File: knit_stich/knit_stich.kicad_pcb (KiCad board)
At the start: 4 copper layers, 89.5 x 65.2 mm, 0 parts

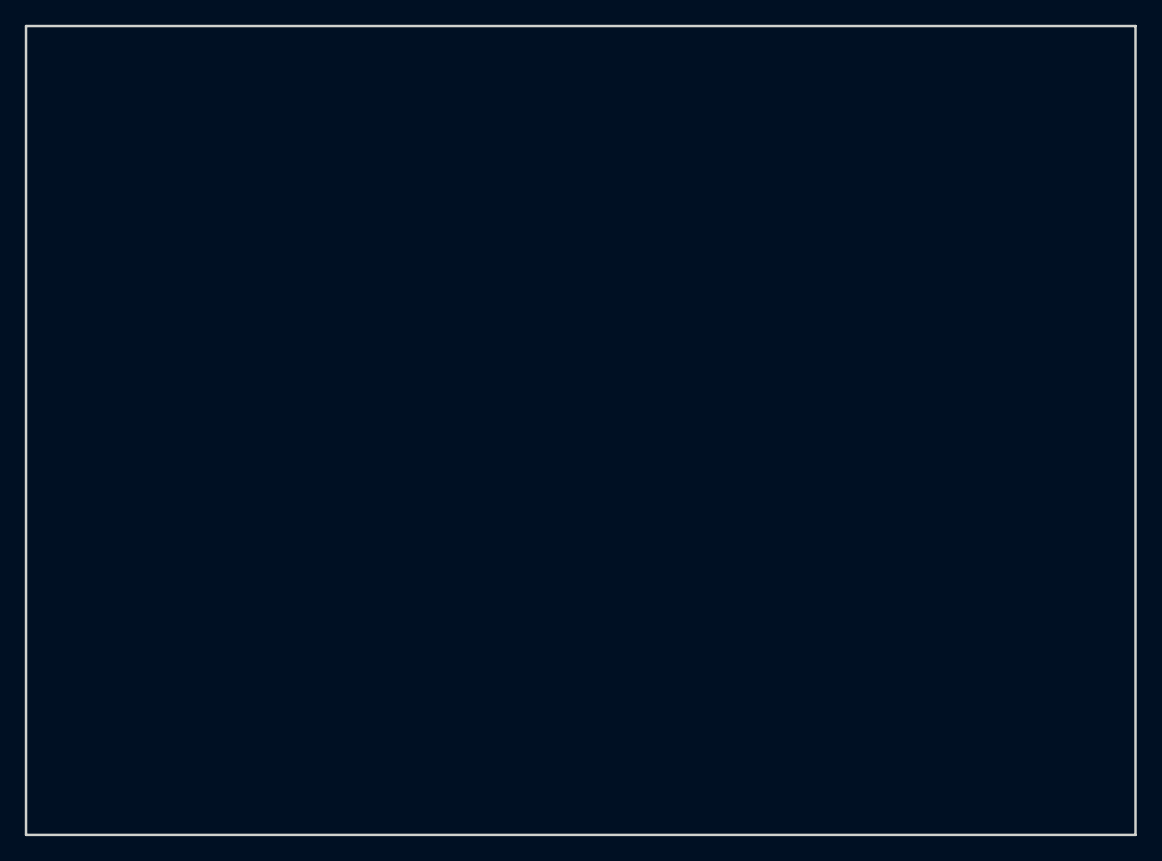
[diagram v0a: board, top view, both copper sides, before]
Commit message: added 2x3 connector
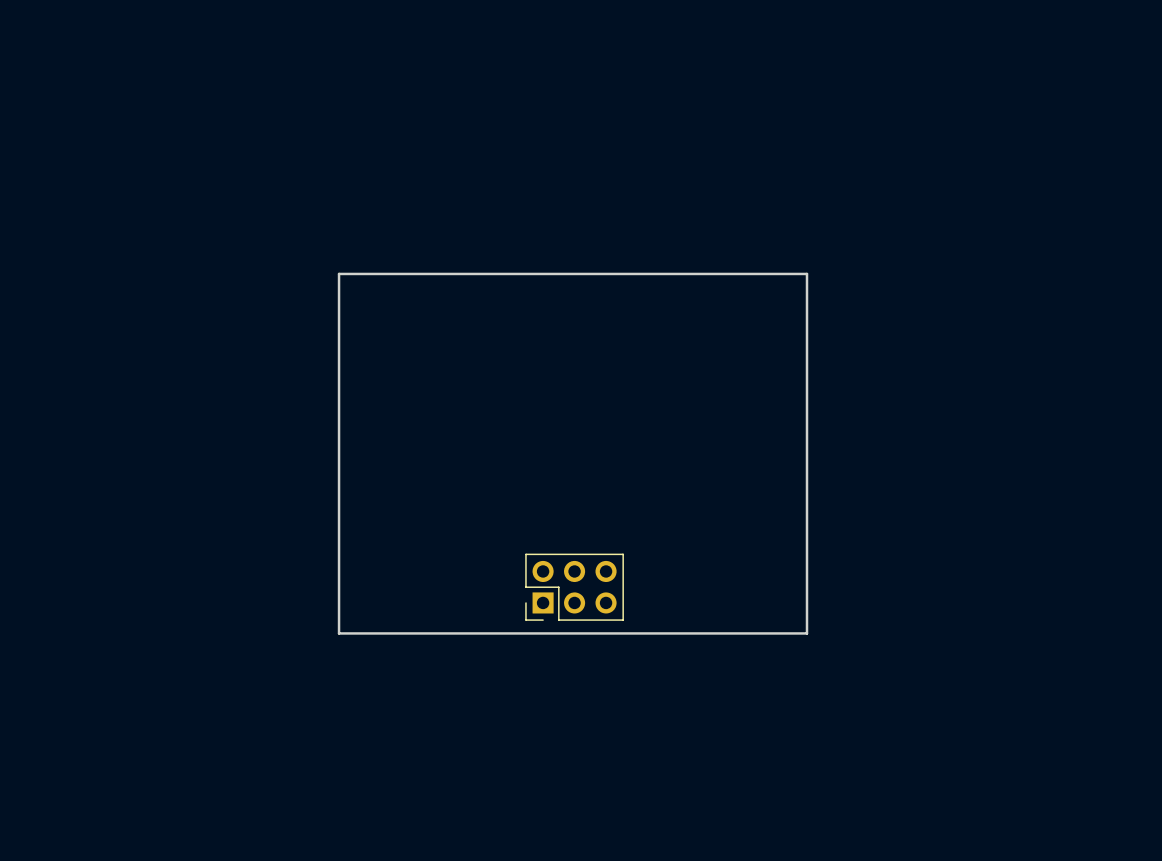
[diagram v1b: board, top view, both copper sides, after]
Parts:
- added J1: Conn_02x03_Counter_Clockwise, Connector_PinHeader_2.54mm:PinHeader_2x03_P2.54mm_Vertical, F.Cu at (158.2, 105.8)
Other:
- board size 89.5 x 65.2 mm -> 37.8 x 29 mm

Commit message: add gitignore
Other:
- board size 37.8 x 29 mm -> 37.2 x 28.2 mm
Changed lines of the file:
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@@
 		(layer "In2.Cu")
 	)
-	(gr_rect
-		(start 141.75 79.25)
-		(end 179.5 108.25)
+	(gr_poly
+		(pts
+			(xy 172.679214 79.411041) (xy 172.875432 79.414604) (xy 173.071511 79.422028) (xy 173.267372 79.434237)
+			(xy 173.462933 79.452156) (xy 173.658117 79.476708) (xy 173.897271 79.513147) (xy 174.133793 79.562787)
+			(xy 174.367398 79.62527) (xy 174.597799 79.700233) (xy 174.824712 79.787317) (xy 175.047851 79.886162)
+			(xy 175.26693 79.996407) (xy 175.481665 80.117691) (xy 175.691769 80.249654) (xy 175.896958 80.391936)
+			(xy 176.291446 80.706013) (xy 176.662846 81.057038) (xy 177.008873 81.442129) (xy 177.327244 81.858401)
+			(xy 177.615676 82.302971) (xy 177.871885 82.772955) (xy 178.093586 83.26547) (xy 178.278498 83.777631)
+			(xy 178.424335 84.306555) (xy 178.528814 84.849359) (xy 178.56483 85.125065) (xy 178.589651 85.403159)
+			(xy 178.613704 88.496238) (xy 178.619149 91.589729) (xy 178.616918 97.776849) (xy 178.60883 98.288336)
+			(xy 178.610099 98.800184) (xy 178.6221 99.824176) (xy 178.62353 100.335926) (xy 178.615711 100.847252)
+			(xy 178.593993 101.357955) (xy 178.553724 101.867841) (xy 178.521001 102.148441) (xy 178.476622 102.425766)
+			(xy 178.420916 102.699481) (xy 178.354209 102.969252) (xy 178.276828 103.234744) (xy 178.189101 103.495622)
+			(xy 178.091355 103.751553) (xy 177.983917 104.0022) (xy 177.867115 104.247229) (xy 177.741275 104.486307)
+			(xy 177.606726 104.719097) (xy 177.463793 104.945266) (xy 177.312806 105.164479) (xy 177.154089 105.3764)
+			(xy 176.987972 105.580697) (xy 176.814781 105.777032) (xy 176.634843 105.965073) (xy 176.448486 106.144485)
+			(xy 176.256036 106.314932) (xy 176.057822 106.47608) (xy 175.85417 106.627595) (xy 175.645408 106.769142)
+			(xy 175.431862 106.900385) (xy 175.213861 107.020991) (xy 174.99173 107.130625) (xy 174.765799 107.228952)
+			(xy 174.536393 107.315638) (xy 174.30384 107.390347) (xy 174.068467 107.452746) (xy 173.830602 107.502499)
+			(xy 173.590572 107.539272) (xy 173.348703 107.56273) (xy 149.886782 107.582055) (xy 149.452176 107.573133)
+			(xy 149.017336 107.574194) (xy 148.147458 107.587189) (xy 147.712674 107.589587) (xy 147.278161 107.582895)
+			(xy 146.844046 107.562343) (xy 146.627177 107.54538) (xy 146.410456 107.523164) (xy 146.16854 107.491112)
+			(xy 145.929226 107.445427) (xy 145.692807 107.386484) (xy 145.459575 107.314657) (xy 145.229822 107.230323)
+			(xy 145.003841 107.133856) (xy 144.781925 107.025631) (xy 144.564366 106.906024) (xy 144.351456 106.77541)
+			(xy 144.143487 106.634164) (xy 143.743546 106.321276) (xy 143.36688 105.970361) (xy 143.01583 105.584423)
+			(xy 142.692736 105.166461) (xy 142.399936 104.719477) (xy 142.139771 104.246473) (xy 141.91458 103.75045)
+			(xy 141.726703 103.234409) (xy 141.578479 102.701352) (xy 141.472247 102.154281) (xy 141.43561 101.876428)
+			(xy 141.410348 101.596196) (xy 141.386236 98.492292) (xy 141.380784 95.387969) (xy 141.383024 89.179183)
+			(xy 141.391341 88.668768) (xy 141.390029 88.157937) (xy 141.377779 87.135922) (xy 141.376471 86.625182)
+			(xy 141.384794 86.114917) (xy 141.407563 85.60535) (xy 141.449593 85.096702) (xy 141.4835 84.817278)
+			(xy 141.52895 84.541165) (xy 141.58562 84.268691) (xy 141.653185 84.000187) (xy 141.731321 83.735983)
+			(xy 141.819704 83.476408) (xy 141.91801 83.221793) (xy 142.025914 82.972468) (xy 142.143093 82.728762)
+			(xy 142.269222 82.491005) (xy 142.403978 82.259529) (xy 142.547036 82.034661) (xy 142.698073 81.816733)
+			(xy 142.856763 81.606075) (xy 143.022784 81.403016) (xy 143.19581 81.207886) (xy 143.375518 81.021016)
+			(xy 143.561584 80.842735) (xy 143.753683 80.673374) (xy 143.951492 80.513261) (xy 144.154687 80.362728)
+			(xy 144.362942 80.222104) (xy 144.575935 80.091719) (xy 144.793341 79.971903) (xy 145.014836 79.862987)
+			(xy 145.240096 79.765299) (xy 145.468797 79.679171) (xy 145.700614 79.604931) (xy 145.935224 79.542911)
+			(xy 146.172303 79.493439) (xy 146.411526 79.456847) (xy 146.652569 79.433463) (xy 172.090525 79.414254)
+			(xy 172.090513 79.414273) (xy 172.482935 79.410414)
+		)
 		(stroke
-			(width 0.2)
+			(width 0.1)
 			(type solid)
+			(color 255 85 85 1)
 		)
 		(fill no)
@@
 		)
 	)
+	(group ""
+		(members "df4445b0-fc9c-452b-98b0-ab519abb0a29")
+	)
 	(embedded_fonts no)

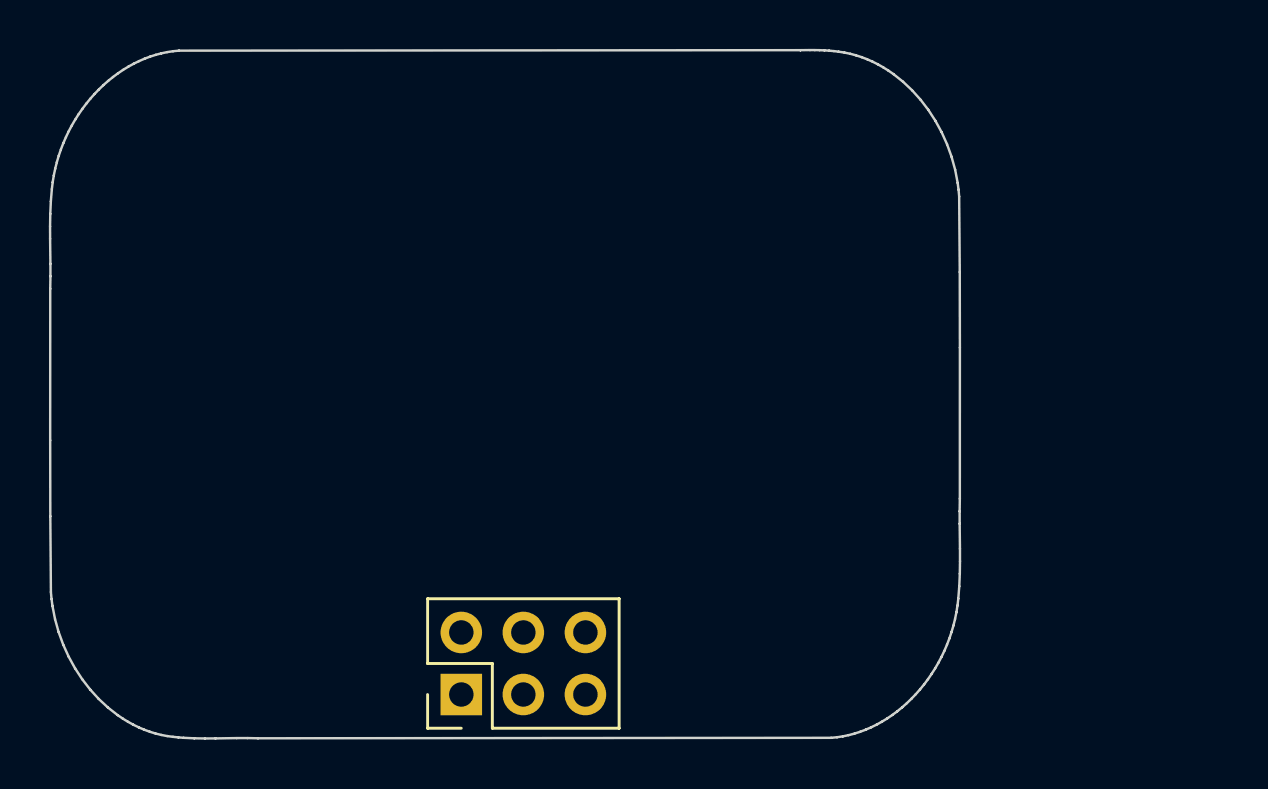
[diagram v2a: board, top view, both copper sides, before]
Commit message: added step for right angle led
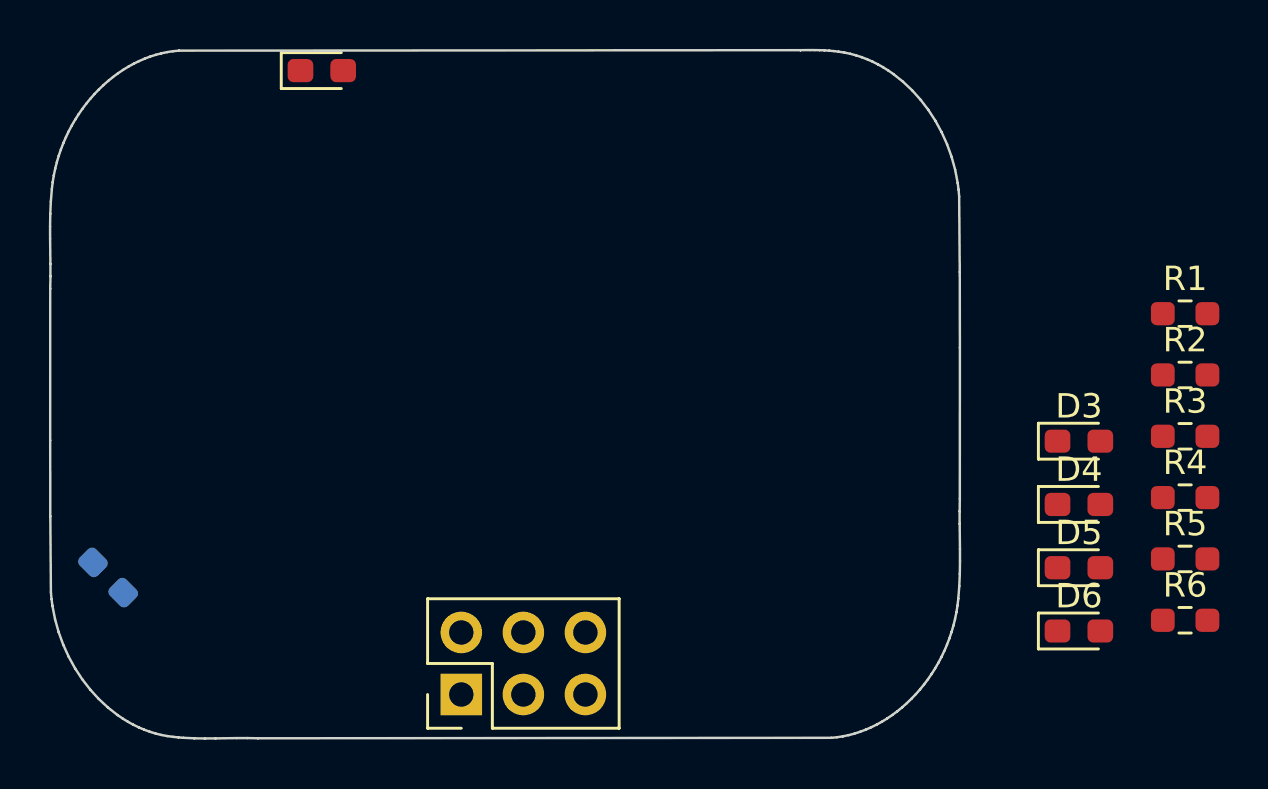
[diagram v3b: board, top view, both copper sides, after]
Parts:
- added D1: LED, LED_SMD:LED_0603_1608Metric_Pad1.05x0.95mm_HandSolder, B.Cu at (143.8, 101.0)
- added D2: LED, LED_SMD:LED_0603_1608Metric_Pad1.05x0.95mm_HandSolder, F.Cu at (152.5, 80.2)
- added D3: LED, LED_SMD:LED_0603_1608Metric_Pad1.05x0.95mm_HandSolder, F.Cu at (183.5, 95.4)
- added D4: LED, LED_SMD:LED_0603_1608Metric_Pad1.05x0.95mm_HandSolder, F.Cu at (183.5, 98.0)
- added D5: LED, LED_SMD:LED_0603_1608Metric_Pad1.05x0.95mm_HandSolder, F.Cu at (183.5, 100.6)
- added D6: LED, LED_SMD:LED_0603_1608Metric_Pad1.05x0.95mm_HandSolder, F.Cu at (183.5, 103.2)
- added R1: R_US, Resistor_SMD:R_0603_1608Metric_Pad0.98x0.95mm_HandSolder, F.Cu at (187.8, 90.2)
- added R2: R_US, Resistor_SMD:R_0603_1608Metric_Pad0.98x0.95mm_HandSolder, F.Cu at (187.8, 92.7)
- added R3: R_US, Resistor_SMD:R_0603_1608Metric_Pad0.98x0.95mm_HandSolder, F.Cu at (187.8, 95.2)
- added R4: R_US, Resistor_SMD:R_0603_1608Metric_Pad0.98x0.95mm_HandSolder, F.Cu at (187.8, 97.7)
- added R5: R_US, Resistor_SMD:R_0603_1608Metric_Pad0.98x0.95mm_HandSolder, F.Cu at (187.8, 100.2)
- added R6: R_US, Resistor_SMD:R_0603_1608Metric_Pad0.98x0.95mm_HandSolder, F.Cu at (187.8, 102.8)
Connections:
- J1 pad 1: unconnected-(J1-Pin_1-Pad1) -> GND
- J1 pad 2: unconnected-(J1-Pin_2-Pad2) -> +3.3V

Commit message: all components in place
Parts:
- D2, D3, D4, D5, D6, R1, R2, R3, R4, R5, R6: moved to B.Cu
- moved R1 45.9 mm to (142.2, 95.2), turned to 90 degrees
- moved R2 40.2 mm to (149.7, 80.0)
- moved R5 38.2 mm to (149.7, 102.2)
- moved D5 29.8 mm to (153.7, 102.2), turned to 180 degrees
- moved R3 23.1 mm to (170.4, 80.0), turned to 180 degrees
- moved D3 23.0 mm to (166.4, 80.0)
- moved R6 17.4 mm to (170.4, 102.2), turned to 180 degrees
- moved D6 17.1 mm to (166.4, 102.2)
- moved R4 10.4 mm to (177.8, 95.2), turned to 90 degrees
- moved D1 9.86 mm to (142.2, 91.2), turned to -90 degrees
- moved D4 8.87 mm to (177.8, 91.2), turned to -90 degrees
- moved D2 1.23 mm to (153.7, 80.0), turned to 180 degrees
- moved J1 0.71 mm to (157.5, 105.8)
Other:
- board size 37.2 x 28.2 mm -> 37.9 x 28.9 mm

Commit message: pcb done
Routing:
- net +3.3V: track 0.00 -> 58.8 mm, vias 0 -> 5
- net GND: track 0.00 -> 10.2 mm, vias 0 -> 6
- net Net-(D1-A): track 0.00 -> 2.21 mm
- net Net-(D6-A): track 0.00 -> 2.21 mm
- net Net-(D4-A): track 0.00 -> 2.21 mm
- net Net-(D3-A): track 0.00 -> 2.21 mm
- net Net-(D5-A): track 0.00 -> 2.21 mm
- net Net-(D2-A): track 0.00 -> 2.21 mm
- added copper zone on B.Cu, net +3.3V
- added copper zone on F.Cu, net GND
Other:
- board text added: "@borisnotes"
- board text added: "KNIT"
- board text added: "STITCH"
- board text added: "Stockholm, SWE 2025/07/28"
